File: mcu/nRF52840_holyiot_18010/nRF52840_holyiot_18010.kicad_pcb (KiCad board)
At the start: 2 copper layers, 3 parts

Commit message: add reset module
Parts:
- removed MCU_SW1: SW_Push, ErgoCai.pretty:K2-1187SQ

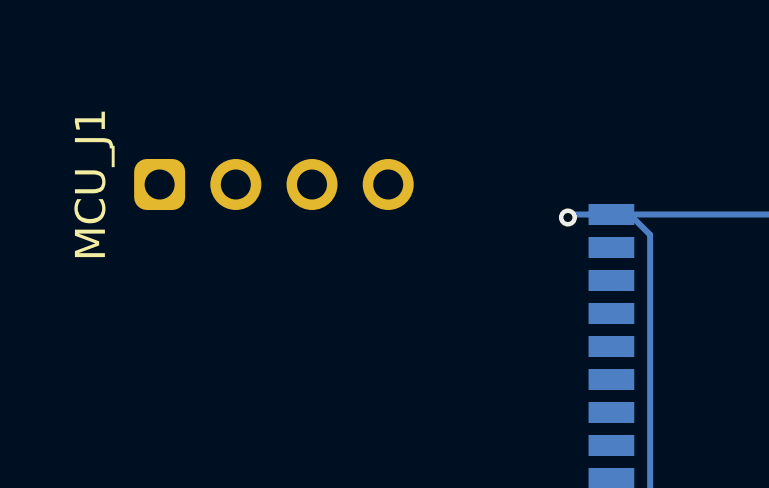
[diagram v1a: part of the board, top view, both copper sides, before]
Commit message: update mcu debug port pos
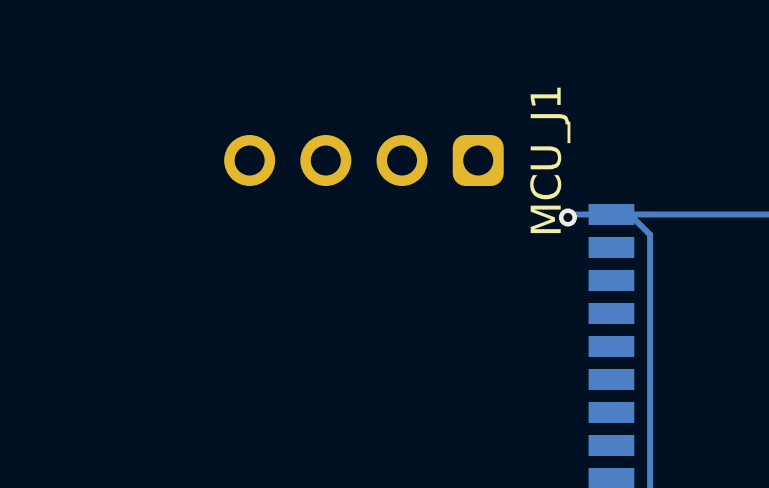
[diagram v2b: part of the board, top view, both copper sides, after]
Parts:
- moved MCU_J1 3.10 mm to (-15.0, -7.50), turned to -90 degrees
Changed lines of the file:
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@@
 	(footprint "ErgoCai.pretty:Connector_THT_1x4_2.54"
 		(layer "F.Cu")
-		(at -18 -6.7 90)
+		(at -15 -7.5 -90)
 		(property "Reference" "MCU_J1"
 			(at 0 -6.096 90)
@@
 		(sheetfile "nRF52840_holyiot_18010.kicad_sch")
 		(fp_line
-			(start 1.27 -5.08)
-			(end 1.27 5.08)
+			(start -1.27 5.08)
+			(end -1.27 -4.445)
+			(stroke
+				(width 0.1)
+				(type solid)
+			)
+			(layer "F.Fab")
+		)
+		(fp_line
+			(start 1.27 5.08)
+			(end -1.27 5.08)
+			(stroke
+				(width 0.1)
+				(type solid)
+			)
+			(layer "F.Fab")
+		)
+		(fp_line
+			(start -1.27 -4.445)
+			(end -0.635 -5.08)
 			(stroke
 				(width 0.1)
@@
 		)
 		(fp_line
-			(start -1.27 -4.445)
-			(end -0.635 -5.08)
-			(stroke
-				(width 0.1)
-				(type solid)
-			)
-			(layer "F.Fab")
-		)
-		(fp_line
-			(start 1.27 5.08)
-			(end -1.27 5.08)
-			(stroke
-				(width 0.1)
-				(type solid)
-			)
-			(layer "F.Fab")
-		)
-		(fp_line
-			(start -1.27 5.08)
-			(end -1.27 -4.445)
+			(start 1.27 -5.08)
+			(end 1.27 5.08)
 			(stroke
 				(width 0.1)
@@
 		)
 		(pad "1" thru_hole roundrect
-			(at 0 -3.81 90)
+			(at 0 -3.81 270)
 			(size 1.7 1.7)
 			(drill 1)
@@
 		)
 		(pad "2" thru_hole oval
-			(at 0 -1.27 90)
+			(at 0 -1.27 270)
 			(size 1.7 1.7)
 			(drill 1)
@@
 		)
 		(pad "3" thru_hole oval
-			(at 0 1.27 90)
+			(at 0 1.27 270)
 			(size 1.7 1.7)
 			(drill 1)
@@
 		)
 		(pad "4" thru_hole oval
-			(at 0 3.81 90)
+			(at 0 3.81 270)
 			(size 1.7 1.7)
 			(drill 1)

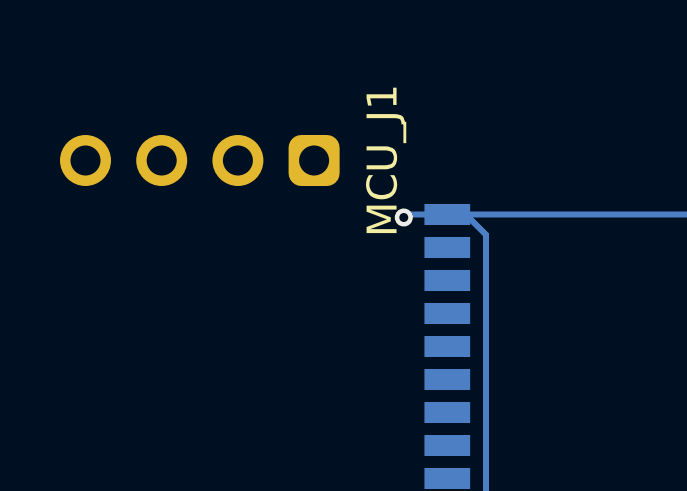
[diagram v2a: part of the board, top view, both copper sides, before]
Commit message: update battery switch symbol
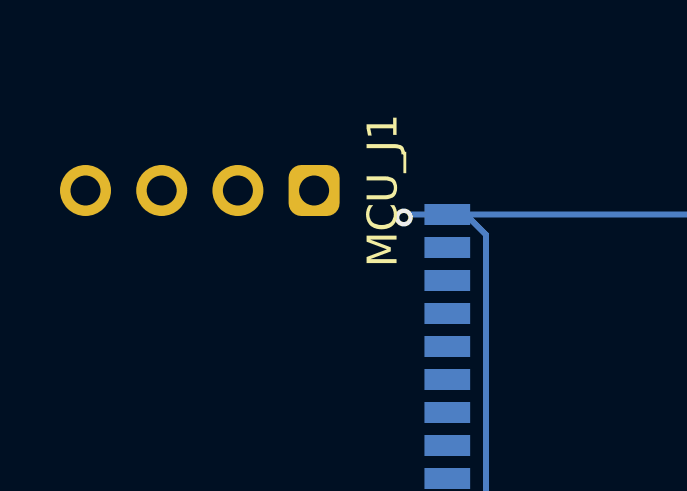
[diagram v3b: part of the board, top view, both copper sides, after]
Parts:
- moved MCU_J1 1.00 mm to (-15.0, -6.50)
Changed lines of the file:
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@@
 	(footprint "ErgoCai.pretty:Connector_THT_1x4_2.54"
 		(layer "F.Cu")
-		(at -15 -7.5 -90)
+		(at -15 -6.5 -90)
 		(property "Reference" "MCU_J1"
 			(at 0 -6.096 90)

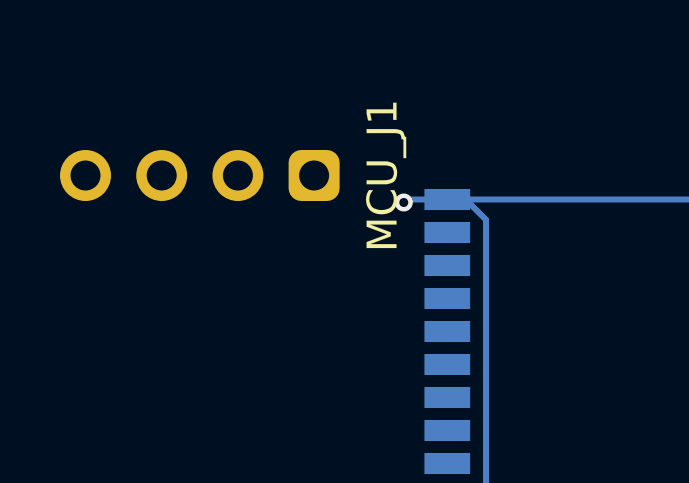
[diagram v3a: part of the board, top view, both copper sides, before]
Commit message: update mcu j1 pos
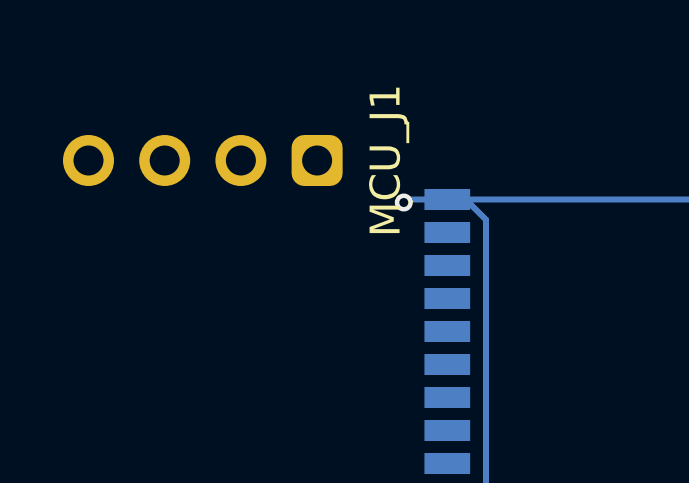
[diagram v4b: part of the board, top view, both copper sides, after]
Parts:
- moved MCU_J1 0.51 mm to (-14.9, -7.00)
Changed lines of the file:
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@@
 	(footprint "ErgoCai.pretty:Connector_THT_1x4_2.54"
 		(layer "F.Cu")
-		(at -15 -6.5 -90)
+		(at -14.9 -7 -90)
 		(property "Reference" "MCU_J1"
 			(at 0 -6.096 90)

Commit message: update to 3.3V tag
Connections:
- net VCC renamed 3.3V
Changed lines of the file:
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@@
 	(net 0 "")
 	(net 1 "SWD")
-	(net 2 "VCC")
+	(net 2 "3.3V")
 	(net 3 "GND")
 	(net 4 "SWC")
@@
 			)
 		)
-		(property "Datasheet" ""
+		(property "Datasheet" "~"
 			(at 0 0 90)
 			(layer "F.Fab")
@@
 			(layers "*.Cu" "*.Mask")
 			(remove_unused_layers no)
-			(net 2 "VCC")
+			(net 2 "3.3V")
 			(pinfunction "Pin_2")
 			(pintype "passive")
@@
 			(size 1.524 0.7)
 			(layers "B.Cu" "B.Mask" "B.Paste")
-			(net 2 "VCC")
+			(net 2 "3.3V")
 			(pinfunction "VDD")
 			(pintype "power_in")
